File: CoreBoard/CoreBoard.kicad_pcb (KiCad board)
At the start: 2 copper layers, 71 parts, among them J1 RJ45_LED_Shielded, SW1 SW_Push, SW10 SW_Push, SW2 SW_Push, SW3 SW_Push, SW4 SW_Push, SW5 SW_Push, SW6 SW_Push, SW7 SW_Push, SW8 SW_Push, SW9 SW_Push, U1 OKI, U2 Teensy4.1_DEV-16771, U4 GY-521, U5 ATA6561, U6 74HC148, U7 74HC148, U8 74HC00

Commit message: Added ground layer to layout
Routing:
- added copper zone on B.Cu, net GND
- added copper zone on F.Cu, net GND
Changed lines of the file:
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@@
+		)
+	)
+	(zone
+		(net 1)
+		(net_name "GND")
+		(layers "F&B.Cu")
+		(hatch edge 0.5)
+		(connect_pads yes
+			(clearance 0.5)
+		)
+		(min_thickness 0.25)
+		(filled_areas_thickness no)
+		(fill
+			(thermal_gap 0.5)
+			(thermal_bridge_width 0.5)
+		)
+		(polygon
+			(pts
+				(xy 302.26 -5.334) (xy -5.08 -5.08) (xy -5.08 215.9) (xy 302.26 215.9)
+			)
 		)
 	)

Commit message: Layout has been changed to group components together similar to the style of the schematic for better connections, and the footprint for the OKI for the NeoPixels has been changed
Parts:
- added U3: SHHD003A0A, MRDT_Devices:SHHD003A0A-SRZ_Surface_Mount, F.Cu at (76.2, 92.2)
- moved R16 245.8 mm to (276.6, 83.5)
- moved R21 242.3 mm to (276.6, 71.0)
- moved D10 241.3 mm to (272.8, 83.5)
- moved R24 240.1 mm to (276.8, 96.0)
- moved D13 239.0 mm to (273.0, 96.0)
- moved R17 238.7 mm to (269.0, 83.5)
- moved R8 237.3 mm to (263.6, 83.5)
- moved D12 236.6 mm to (272.8, 71.0)
- moved R18 236.5 mm to (263.6, 71.0)
- moved R10 236.0 mm to (263.4, 96.0)
- moved R20 234.4 mm to (269.0, 71.0)
- moved R25 232.8 mm to (269.2, 96.0)
- moved D7 230.4 mm to (259.6, 96.0)
- moved R9 230.2 mm to (256.0, 83.5)
- moved R19 229.7 mm to (256.0, 71.0)
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
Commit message: Rearranged layout for better off-board wire arrangement
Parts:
- added H1: MountingHole, MRDT_Drill_Holes:4_40_Hole, F.Cu at (55.6, 42.2)
- added H2: MountingHole, MRDT_Drill_Holes:4_40_Hole, F.Cu at (21.1, 28.4)
- added H3: MountingHole, MRDT_Drill_Holes:4_40_Hole, F.Cu at (21.1, 37.5)
- added H4: MountingHole, MRDT_Drill_Holes:4_40_Hole, F.Cu at (54.4, 124.0)
- moved Conn8 172.3 mm to (85.4, 22.7), turned to 0 degrees
- moved Conn9 163.9 mm to (95.0, 22.6), turned to 0 degrees
- moved C6 156.6 mm to (92.0, 32.4), turned to 90 degrees
- moved U5 156.2 mm to (92.0, 42.9), turned to 90 degrees
- moved R22 151.5 mm to (87.2, 35.7)
- moved C4 146.7 mm to (96.1, 50.7), turned to -90 degrees
- moved D13 145.4 mm to (129.6, 119.6)
- moved D4 145.4 mm to (103.5, 94.6)
- moved D7 145.4 mm to (116.1, 119.6)
- moved D8 145.4 mm to (103.4, 119.6)
- moved D9 145.4 mm to (103.5, 107.1)
- moved R10 145.4 mm to (119.9, 119.6)
- moved R11 145.4 mm to (112.3, 119.6)
- moved R12 145.4 mm to (107.2, 119.6)
- moved R13 145.4 mm to (99.6, 119.6)
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
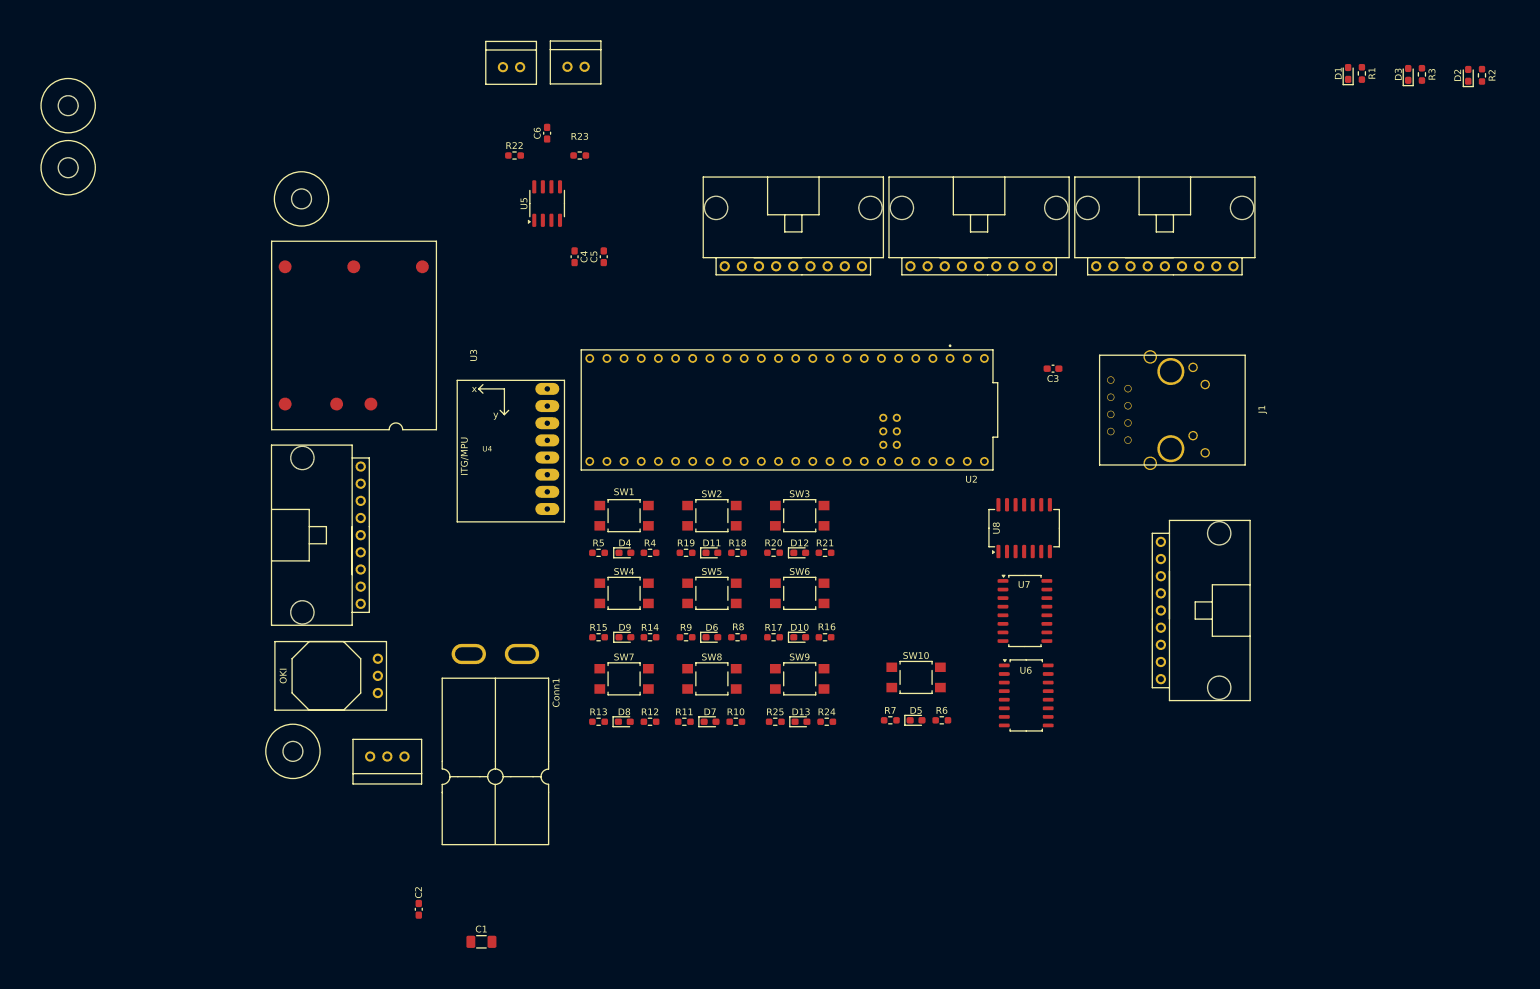
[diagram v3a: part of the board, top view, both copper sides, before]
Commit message: Changed footprint of NeoPixels to a though hole, and added some wires
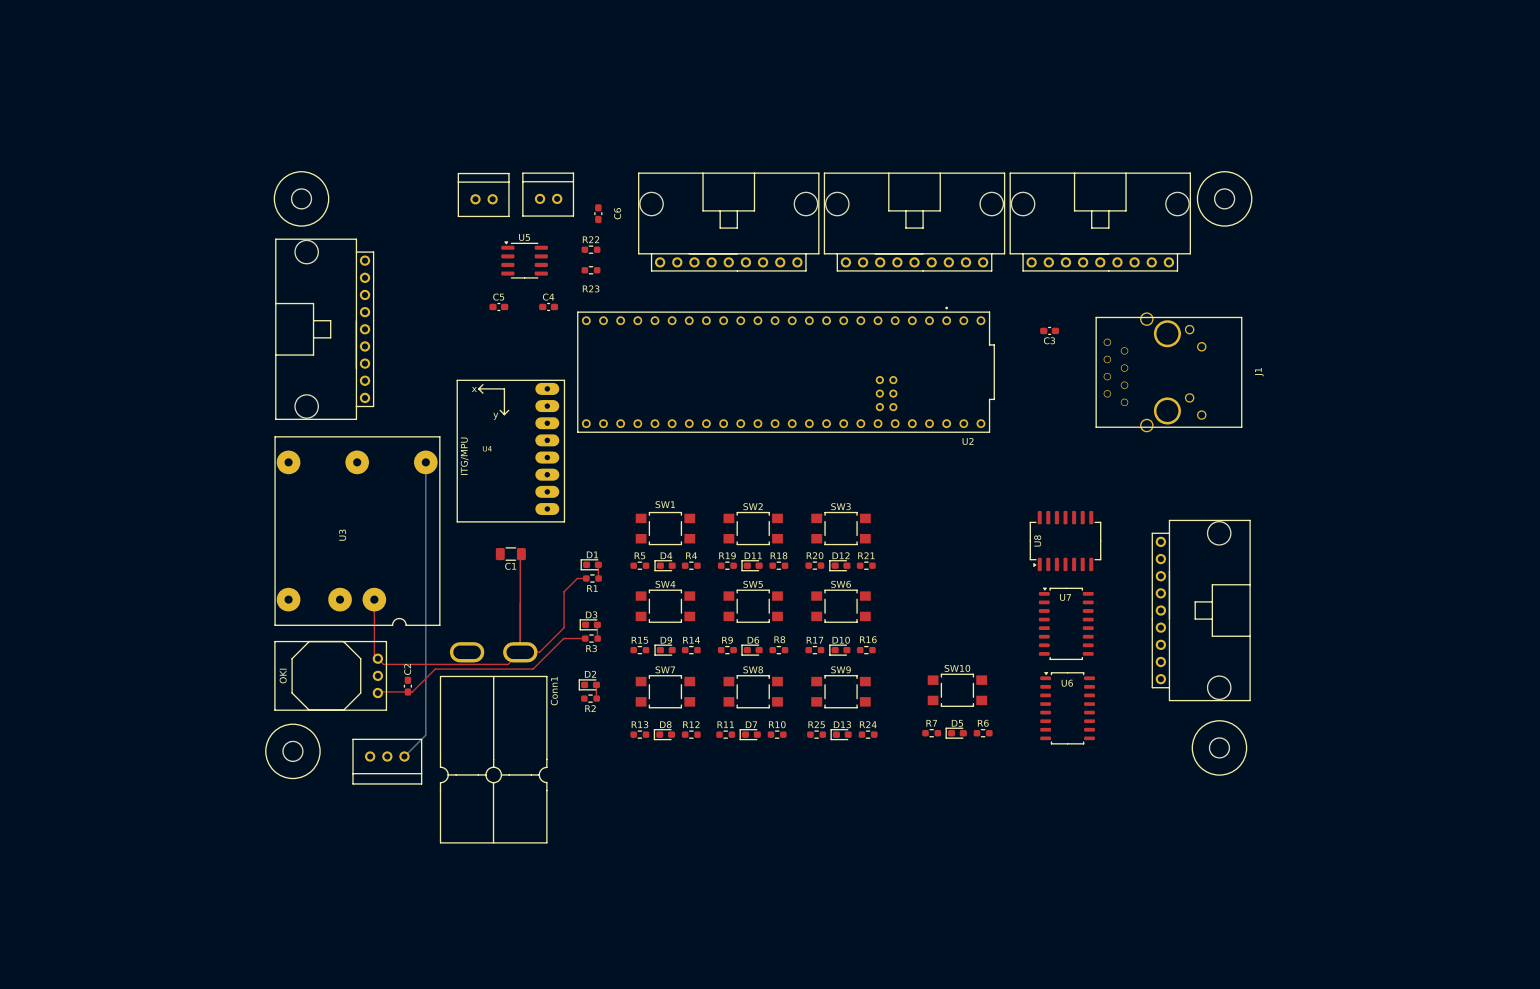
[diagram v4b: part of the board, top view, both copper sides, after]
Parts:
- U3: footprint MRDT_Devices:SHHD003A0A-SRZ_Surface_Mount -> MRDT_Devices:SHHD003A0A41Z_Through_Hole
- moved H3 190.9 mm to (191.5, 123.4)
- moved H2 171.8 mm to (192.3, 42.2)
- moved R2 161.0 mm to (98.4, 116.1), turned to 0 degrees
- moved D2 158.2 mm to (98.4, 114.1), turned to 0 degrees
- moved R3 148.6 mm to (98.6, 107.3), turned to 0 degrees
- moved D3 145.8 mm to (98.6, 105.2), turned to 0 degrees
- moved R1 136.3 mm to (98.7, 98.4), turned to 0 degrees
- moved D1 133.4 mm to (98.7, 96.3), turned to 0 degrees
- moved C1 57.6 mm to (86.6, 94.7), turned to 180 degrees
- moved C2 33.1 mm to (71.4, 114.3)
- moved Conn3 30.5 mm to (65.0, 71.6)
- moved U3 29.0 mm to (76.1, 105.3)
- moved Conn9 20.0 mm to (90.9, 42.2)
- moved Conn8 20.0 mm to (81.4, 42.2)
- moved R22 18.0 mm to (98.5, 49.7)
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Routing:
- net VCC: track 0.00 -> 70.5 mm
- net /5V: track 0.00 -> 44.9 mm
- net +5V: track 0.00 -> 34.1 mm
- net Net-(D1-A): track 0.00 -> 2.05 mm
- net Net-(D3-A): track 0.00 -> 2.05 mm
- net Net-(D2-A): track 0.00 -> 2.05 mm

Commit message: Nearly completed first draft of the layout, and adjusted the schematic for easier routing
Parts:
- added SW11: SW_Wuerth_450301014042, MRDT_Switches:SW_Switch_03_STSSS9121_Through_Hole, F.Cu at (145.5, 117.1)
- added SW12: SW_Wuerth_450301014042, MRDT_Switches:SW_Switch_03_STSSS9121_Through_Hole, F.Cu at (145.5, 104.7)
- added SW13: SW_Wuerth_450301014042, MRDT_Switches:SW_Switch_03_STSSS9121_Through_Hole, F.Cu at (145.5, 92.5)
- added SW14: SW_Wuerth_450301014042, MRDT_Switches:SW_Switch_03_STSSS9121_Through_Hole, F.Cu at (151.1, 117.1)
- added SW15: SW_Wuerth_450301014042, MRDT_Switches:SW_Switch_03_STSSS9121_Through_Hole, F.Cu at (151.1, 104.7)
- added SW16: SW_Wuerth_450301014042, MRDT_Switches:SW_Switch_03_STSSS9121_Through_Hole, F.Cu at (151.1, 92.5)
- added SW17: SW_Wuerth_450301014042, MRDT_Switches:SW_Switch_03_STSSS9121_Through_Hole, F.Cu at (156.7, 104.7)
- moved Conn5 55.1 mm to (163.8, 51.6)
- moved Conn7 55.0 mm to (108.7, 51.6)
- moved SW7 28.8 mm to (135.4, 102.6)
- moved SW2 27.3 mm to (135.4, 115.1)
- moved SW6 26.0 mm to (109.5, 102.6)
- moved SW9 25.0 mm to (135.4, 90.2)
- moved SW8 25.0 mm to (122.4, 90.2)
- moved C6 19.9 mm to (80.0, 47.8), turned to 0 degrees
- moved R23 18.7 mm to (80.0, 50.0), turned to 0 degrees
- moved R22 18.6 mm to (80.0, 52.1), turned to 180 degrees
- moved SW5 18.1 mm to (109.5, 115.1)
- moved SW4 18.1 mm to (122.4, 115.1)
- moved SW3 17.5 mm to (122.4, 102.6)
- moved U4 11.1 mm to (89.4, 88.4), turned to 0 degrees
- moved C1 8.13 mm to (86.6, 102.9)
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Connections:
- U2 pad 10: unconnected-(U2-CS1-Pad10) -> DS7
- U2 pad 11: DS6 -> NeoPixels
- U2 pad 12: DS7 -> DS6
- U6 pad 10: B8 -> DS_EN
- U6 pad 12: DS_EN -> B6
- U7 pad 1: B4 -> B2
- U7 pad 11: B1 -> B7
- U7 pad 12: B2 -> B4
- U7 pad 13: B3 -> B1
- U7 pad 3: B6 -> B8
- U7 pad 4: B7 -> B3
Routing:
- net +3.3V: track 0.00 -> 486.1 mm, vias 0 -> 9
- net +5V: track 34.1 -> 382.1 mm, vias 0 -> 7
- net DS2: track 0.00 -> 129.3 mm
- net Out3: track 0.00 -> 127.1 mm, vias 0 -> 4
- net B7: track 0.00 -> 125.0 mm
- net DS3: track 0.00 -> 122.6 mm
- net DS1: track 0.00 -> 120.4 mm, vias 0 -> 2
- net NeoPixels: track 0.00 -> 116.1 mm, vias 0 -> 3
- net B4: track 0.00 -> 112.2 mm
- net B9: track 0.00 -> 107.2 mm
- net DS4: track 0.00 -> 102.6 mm, vias 0 -> 3
- net B8: track 0.00 -> 99.4 mm
- net B1: track 0.00 -> 99.4 mm
- net B6: track 0.00 -> 94.2 mm
- net Out2: track 0.00 -> 93.8 mm, vias 0 -> 4
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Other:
- board outline added: 144.8 x 89.5 mm
- board text added: "BL"
- board text added: "BR"
- board text added: "FL"
- board text added: "FR"
- board text added: "Forward"
- board text added: "ML"
- board text added: "MR"
- board text added: "OFF"
- board text added: "ON"
- board text added: "Reverse"

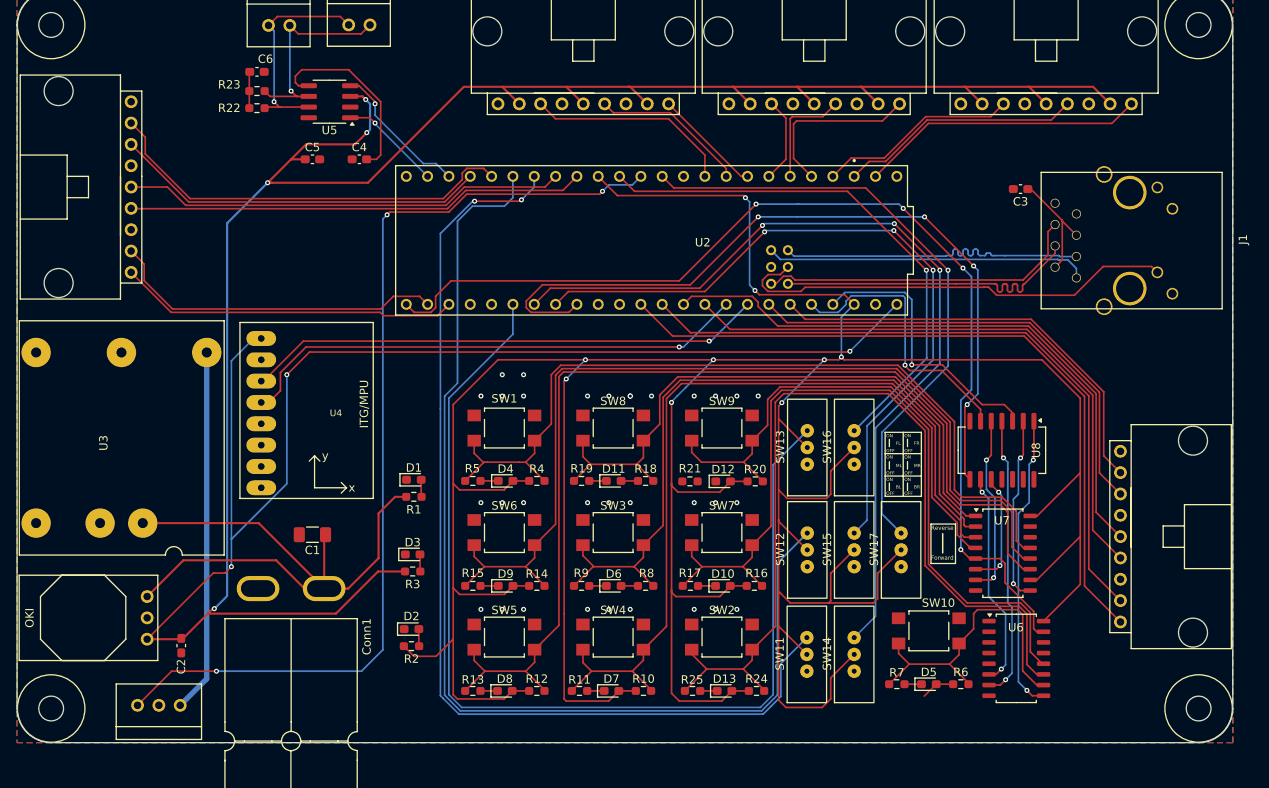
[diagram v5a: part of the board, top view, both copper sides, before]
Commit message: Fixed 90 degree traces, finished routing unconnected traces, placed ground vias to connect other unrouted traces/pads, and added silkscreen labels and header to the layout
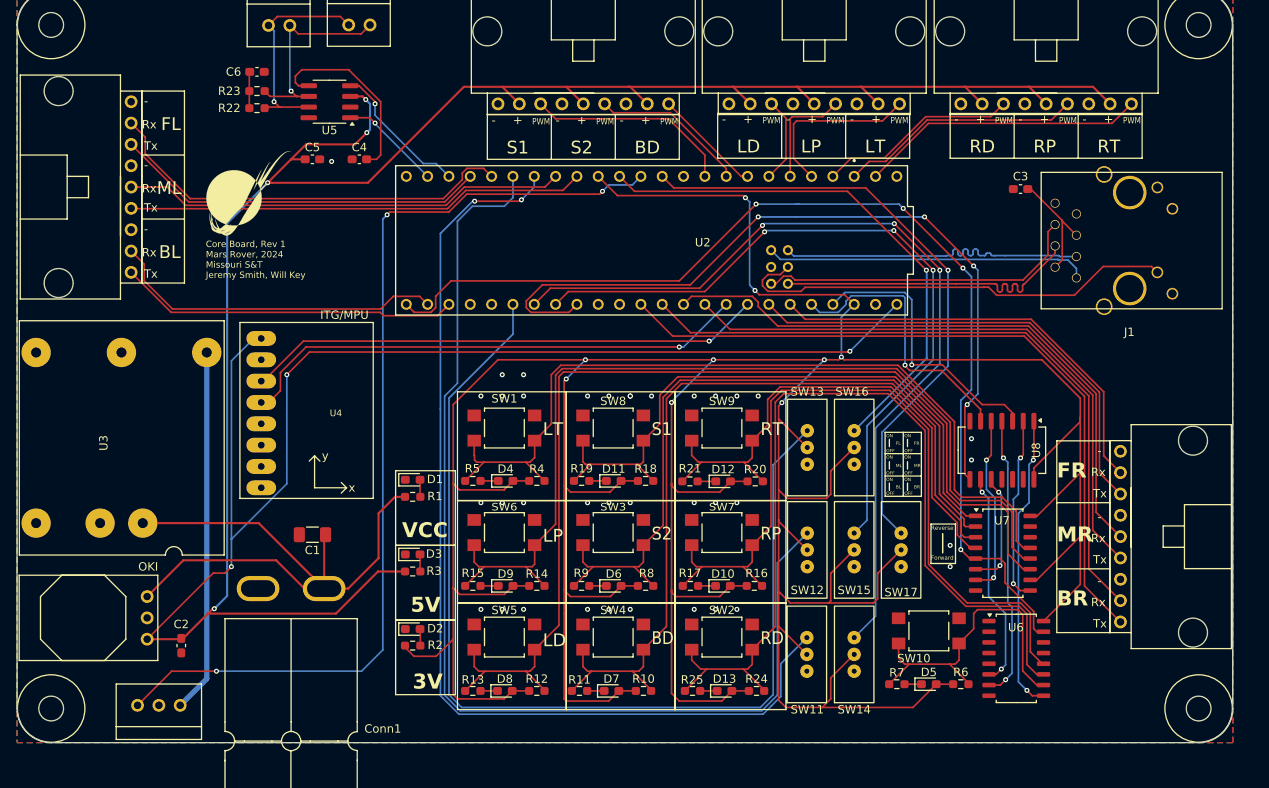
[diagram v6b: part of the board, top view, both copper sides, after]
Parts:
- added G***: LOGO, MRDT_Silkscreens:0_MRDT_Logo_10mm, F.Cu at (79.0, 62.2)
- moved R2 0.15 mm to (98.6, 116.1)
- moved D2 0.14 mm to (98.6, 114.1)
- moved D1 0.14 mm to (98.6, 96.3)
- moved R1 0.14 mm to (98.6, 98.4)
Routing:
- net +3.3V: track 486.1 -> 523.8 mm
- net B3: track 59.1 -> 62.8 mm
- net Net-(D12-K): track 0.00 -> 2.16 mm
- net B4: track 112.2 -> 113.0 mm
- net B1: track 99.4 -> 100.1 mm
- net B9: track 107.2 -> 108.0 mm
- net B8: track 99.4 -> 100.1 mm
- net B7: track 125.0 -> 125.7 mm
- net B6: track 94.2 -> 94.9 mm
- net B5: track 86.5 -> 87.2 mm
- net DS_EN: track 37.9 -> 38.6 mm
- net B2: track 73.8 -> 74.4 mm
- net GND: vias 32 -> 37
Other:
- board text added: "+"
- board text added: "-"
- board text added: "3V"
- board text added: "5V"
- board text added: "BD"
- board text added: "Core Board, Rev 1 Mars Rover, 2024 Missouri S&T Jeremy Smith, Will Key"
- board text added: "LD"
- board text added: "LP"
- board text added: "LT"
- board text added: "Molex_SL_09"
- board text added: "PWM"
- board text added: "RD"
- board text added: "RP"
- board text added: "RT"
- board text added: "Rx"
- board text added: "S1"
- board text added: "S2"
- board text added: "Tx"
- board text added: "VCC"
